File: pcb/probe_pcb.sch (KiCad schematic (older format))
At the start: 47 parts, among them J1 USB_B, J2 USB_B, J3 CONN_01X02, J4 CONN_01X02, J5 CONN_02X20, Q1 MMBT3904, Q2 MMBT3904, Q3 MMBT3904, Q4 MMBT3904, Q5 MMBT3904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

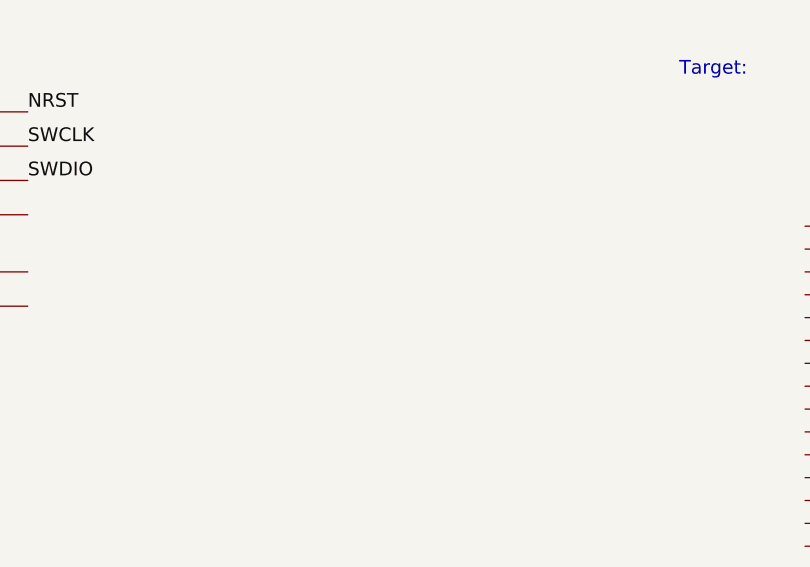
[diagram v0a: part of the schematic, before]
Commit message: Started associating footprints
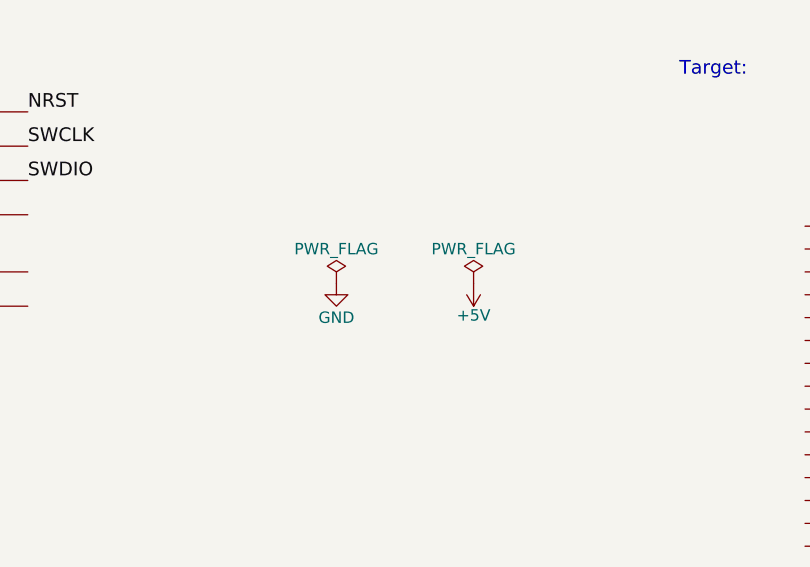
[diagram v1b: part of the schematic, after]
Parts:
- C1, C2, C3, C4: footprint (none) -> Capacitors_SMD:C_0805_HandSoldering
- D1, D2, D3, D4: footprint (none) -> LEDs:LED_0805_HandSoldering
- DS1, DS2, DS3: footprint WC1602A -> Displays:WC1602A
- J1, J2: footprint (none) -> Connectors:USB_B
- J3, J4: footprint (none) -> Pin_Headers:Pin_Header_Angled_1x02_Pitch2.54mm
- J5: footprint (none) -> Pin_Headers:Pin_Header_Angled_2x20_Pitch2.54mm
- Q1, Q2, Q3, Q4, Q5, Q6, Q7, Q8: footprint TO_SOT_Packages_SMD:SOT-23 -> TO_SOT_Packages_SMD:SOT-23_Handsoldering
- R1, R10, R11, R12, R13, R14, R2, R3, R4, R5, R6, R7, R8, R9: footprint (none) -> Resistors_SMD:R_0805_HandSoldering
- RV1: footprint (none) -> Air_Coils_SML_NEOSID:Neosid_Air-Coil_SML_5turn_HDM0531A
- RV2: footprint (none) -> Potentiometers:Potentiometer_Trimmer-EVM3E
- Y1: footprint (none) -> Crystals:Crystal_DS10_d1.0mm_l4.3mm_Horizontal

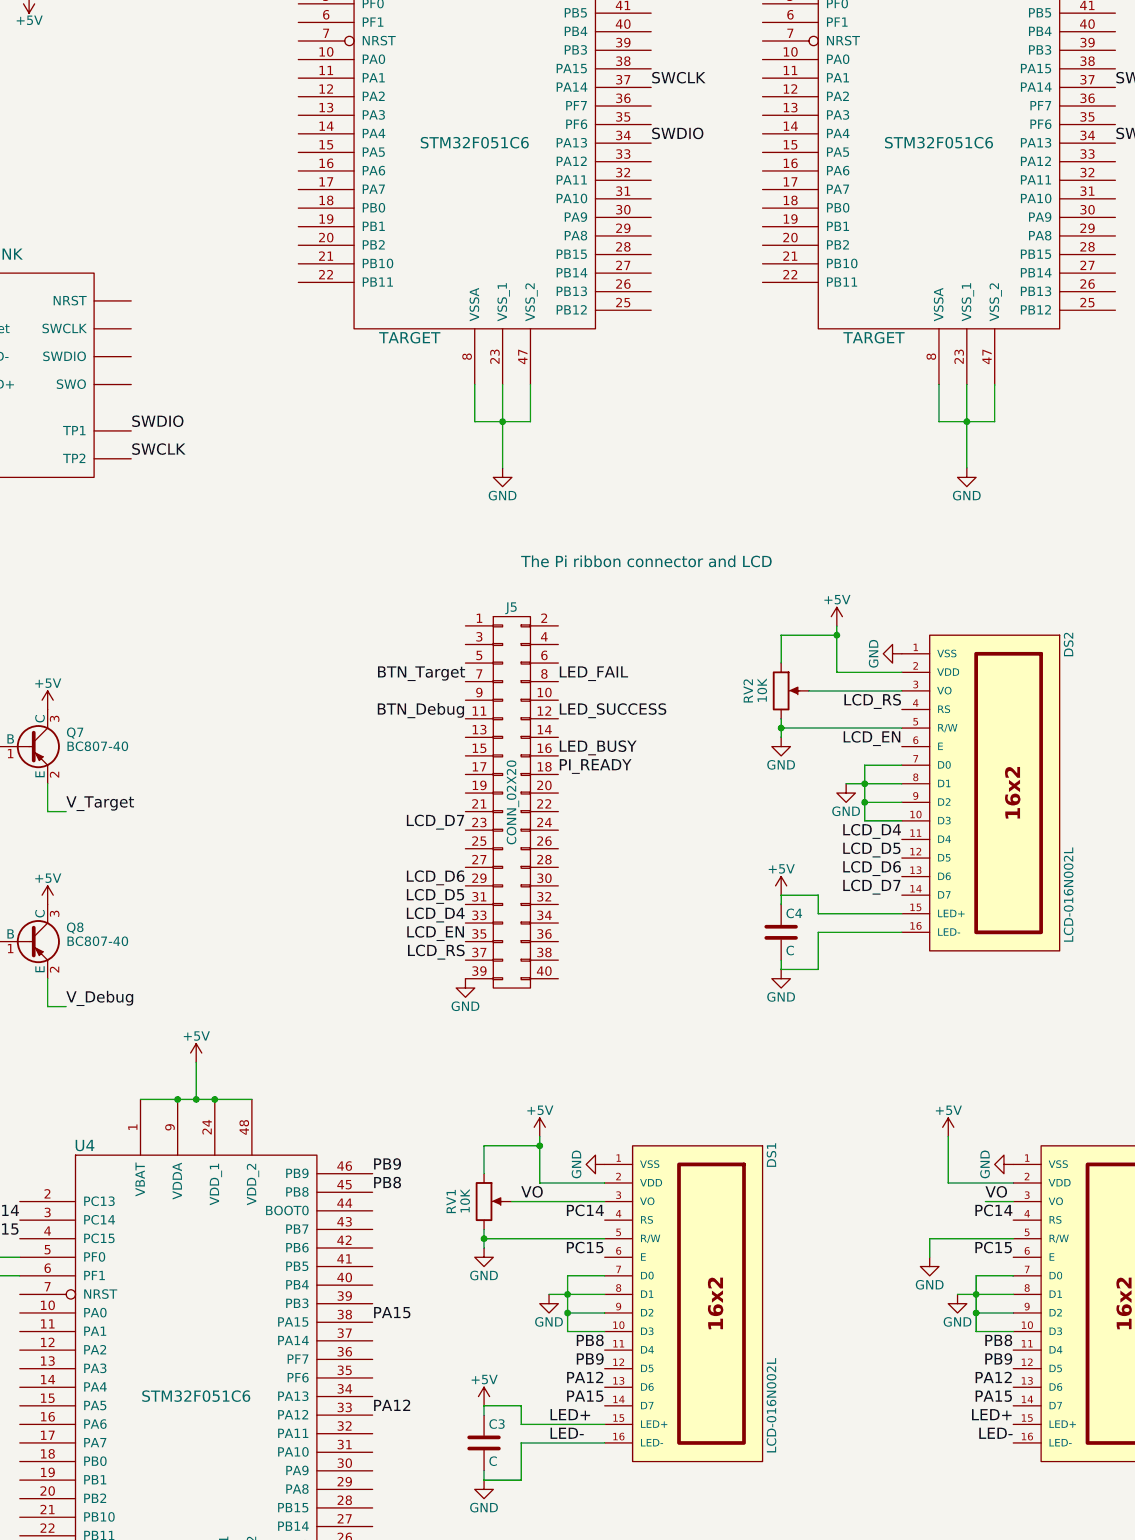
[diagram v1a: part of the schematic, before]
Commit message: Late night commit. Remember: f2_5 NOT 2_4 -> that's why re-encryption wasn't working, silly
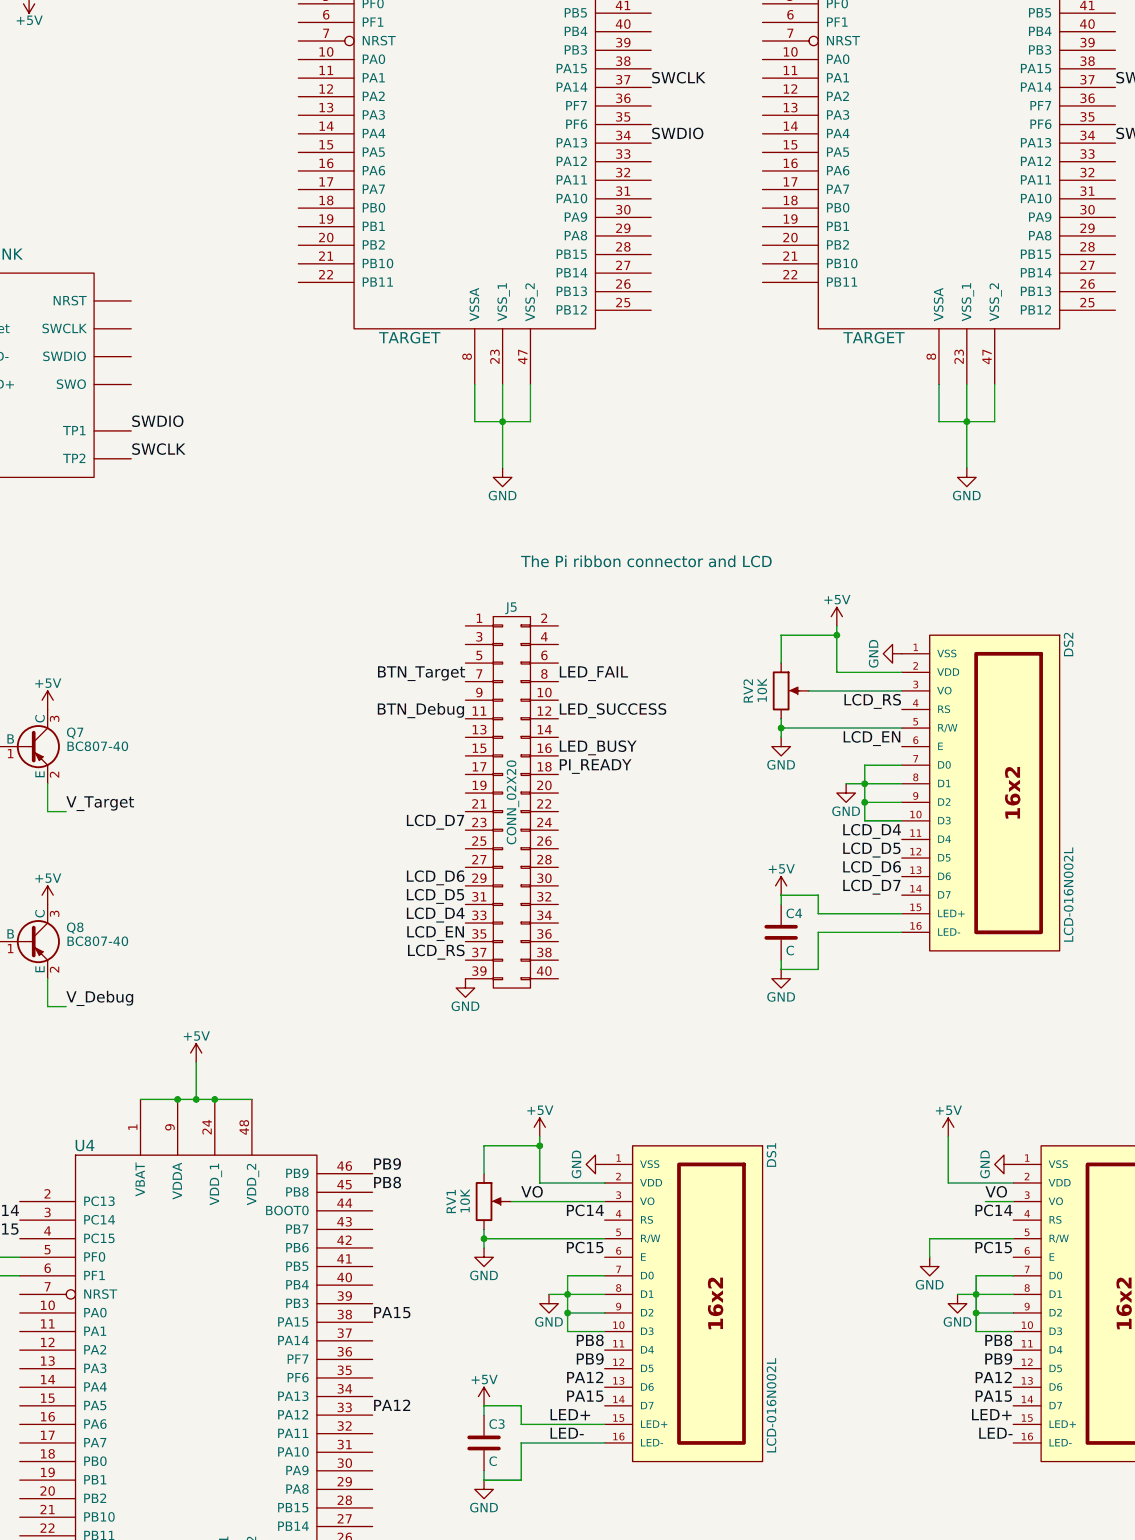
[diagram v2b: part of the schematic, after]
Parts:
- RV1: footprint Air_Coils_SML_NEOSID:Neosid_Air-Coil_SML_5turn_HDM0531A -> Potentiometers:Potentiometer_Alps_RK09L_Single_Vertical
- RV2: footprint Potentiometers:Potentiometer_Trimmer-EVM3E -> Potentiometers:Potentiometer_Alps_RK09L_Single_Vertical
- U4, U5, U6: footprint STM32F051C6 -> (none)
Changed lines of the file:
@@
 LIBS:valves
 LIBS:stm_jig_lib
-LIBS:raspberrypi-gpio-cache
 LIBS:probe_pcb-cache
 EELAYER 25 0
@@
 F 0 "U5" H 7800 3900 60  0000 C CNN
 F 1 "TARGET" H 8050 1500 60  0000 C CNN
-F 2 "STM32F051C6" H 8400 2550 60  0000 C CNN
+F 2 "" H 8400 2550 60  0000 C CNN
 F 3 "" H 8400 2700 60  0001 C CNN
 	1    8650 2650
@@
 F 0 "U4" H 6300 10650 60  0000 C CNN
 F 1 "TARGET" H 6550 8250 60  0000 C CNN
-F 2 "STM32F051C6" H 6900 9300 60  0000 C CNN
+F 2 "" H 6900 9300 60  0000 C CNN
 F 3 "" H 6900 9450 60  0001 C CNN
 	1    7150 9400
@@
 F 0 "RV1" V 8275 8450 50  0000 C CNN
 F 1 "10K" V 8350 8450 50  0000 C CNN
-F 2 "Air_Coils_SML_NEOSID:Neosid_Air-Coil_SML_5turn_HDM0531A" H 8450 8450 50  0001 C CNN
+F 2 "Potentiometers:Potentiometer_Alps_RK09L_Single_Vertical" H 8450 8450 50  0001 C CNN
 F 3 "" H 8450 8450 50  0001 C CNN
 	1    8450 8450
@@
 F 0 "U6" H 10300 3900 60  0000 C CNN
 F 1 "TARGET" H 10550 1500 60  0000 C CNN
-F 2 "STM32F051C6" H 10900 2550 60  0000 C CNN
+F 2 "" H 10900 2550 60  0000 C CNN
 F 3 "" H 10900 2700 60  0001 C CNN
 	1    11150 2650
@@
 F 0 "RV2" V 9875 5700 50  0000 C CNN
 F 1 "10K" V 9950 5700 50  0000 C CNN
-F 2 "Potentiometers:Potentiometer_Trimmer-EVM3E" H 10050 5700 50  0001 C CNN
+F 2 "Potentiometers:Potentiometer_Alps_RK09L_Single_Vertical" H 10050 5700 50  0001 C CNN
 F 3 "" H 10050 5700 50  0001 C CNN
 	1    10050 5700
